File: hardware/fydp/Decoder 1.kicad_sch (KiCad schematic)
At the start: 26 parts, among them J21 Conn_01x04_Pin, J6 Conn_01x04_Pin, U4 74HC139N

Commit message: Did some work in class lol
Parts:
- removed J21, J6: Conn_01x04_Pin, Connector_PinHeader_2.54mm:PinHeader_1x04_P2.54mm_Vertical, symbol Connector:Conn_01x04_Pin
- added J8: Conn_01x08_Pin, Connector_PinHeader_2.54mm:PinHeader_1x08_P2.54mm_Vertical, symbol Connector:Conn_01x08_Pin
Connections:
- net +3.3V: now also J8.5 (Pin_5), J8.7 (Pin_7)
- net ADC_DECODER_A0: now also J8.2 (Pin_2)
- net ADC_DECODER_A1: now also J8.1 (Pin_1)
- net ADC_DECODER_EN_L: now also J8.6 (Pin_6)
- net DAC_IN_DECODER_A0: now also J8.4 (Pin_4)
- net DAC_IN_DECODER_A1: now also J8.3 (Pin_3)
- net DAC_IN_DECODER_EN_L: now also J8.8 (Pin_8)
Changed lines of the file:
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@@
 (kicad_sch (version 20230121) (generator eeschema)
   (paper "A4")
-  (junction (at 196.85 45.72) (diameter 0) (color 0 0 0 0)
-  )
   (junction (at 27.94 140.97) (diameter 0) (color 0 0 0 0)
   )
@@
   (junction (at 52.07 105.41) (diameter 0) (color 0 0 0 0)
   )
+  (junction (at 218.44 57.15) (diameter 0) (color 0 0 0 0)
+  )
   (junction (at 124.46 66.04) (diameter 0) (color 0 0 0 0)
   )
@@
     (stroke (width 0) (type default))
   )
-  (wire (pts (xy 196.85 50.8) (xy 198.12 50.8))
+  (wire (pts (xy 218.44 62.23) (xy 261.62 62.23))
     (stroke (width 0) (type default))
   )
@@
     (stroke (width 0) (type default))
   )
+  (wire (pts (xy 218.44 57.15) (xy 261.62 57.15))
+    (stroke (width 0) (type default))
+  )
   (wire (pts (xy 36.83 151.13) (xy 64.77 151.13))
     (stroke (width 0) (type default))
@@
     (stroke (width 0) (type default))
   )
-  (wire (pts (xy 175.26 48.26) (xy 198.12 48.26))
+  (wire (pts (xy 238.76 59.69) (xy 261.62 59.69))
     (stroke (width 0) (type default))
   )
@@
     (stroke (width 0) (type default))
   )
-  (wire (pts (xy 193.04 44.45) (xy 193.04 45.72))
+  (wire (pts (xy 218.44 44.45) (xy 218.44 57.15))
     (stroke (width 0) (type default))
   )
@@
     (stroke (width 0) (type default))
   )
-  (wire (pts (xy 196.85 45.72) (xy 196.85 50.8))
+  (wire (pts (xy 218.44 57.15) (xy 218.44 62.23))
     (stroke (width 0) (type default))
   )
@@
     (stroke (width 0) (type default))
   )
-  (wire (pts (xy 198.12 45.72) (xy 196.85 45.72))
-    (stroke (width 0) (type default))
-  )
   (wire (pts (xy 217.17 107.95) (xy 217.17 129.54))
     (stroke (width 0) (type default))
@@
     (stroke (width 0) (type default))
   )
-  (wire (pts (xy 196.85 45.72) (xy 193.04 45.72))
-    (stroke (width 0) (type default))
-  )
   (wire (pts (xy 74.93 130.81) (xy 72.39 130.81))
     (stroke (width 0) (type default))
@@
     (stroke (width 0) (type default))
   )
-  (wire (pts (xy 175.26 53.34) (xy 198.12 53.34))
+  (wire (pts (xy 238.76 64.77) (xy 261.62 64.77))
     (stroke (width 0) (type default))
   )
@@
     (stroke (width 0) (type default))
   )
-  (rectangle (start 213.36 31.75) (end 276.86 59.69)
+  (rectangle (start 213.36 31.75) (end 276.86 67.31)
     (stroke (width 0) (type default))
     (fill (type none))
@@
     (effects (font (size 1.27 1.27)) (justify left bottom))
   )
-  (label "ADC_DECODER_A0" (at 223.52 52.07 0) (fields_autoplaced)
-    (effects (font (size 1.27 1.27)) (justify left bottom))
-  )
   (label "ADC4_CS_L_R" (at 95.25 118.11 0) (fields_autoplaced)
     (effects (font (size 1.27 1.27)) (justify left bottom))
@@
     (effects (font (size 1.27 1.27)) (justify left bottom))
   )
-  (label "DAC_IN_DECODER_A0" (at 223.52 46.99 0) (fields_autoplaced)
-    (effects (font (size 1.27 1.27)) (justify left bottom))
-  )
   (label "ADC_DECODER_EN_L" (at 95.25 102.87 0) (fields_autoplaced)
     (effects (font (size 1.27 1.27)) (justify left bottom))
   )
+  (label "ADC_DECODER_A1" (at 223.52 46.99 0) (fields_autoplaced)
+    (effects (font (size 1.27 1.27)) (justify left bottom))
+  )
   (label "ADC2_CS_L_R" (at 95.25 113.03 0) (fields_autoplaced)
     (effects (font (size 1.27 1.27)) (justify left bottom))
@@
     (effects (font (size 1.27 1.27)) (justify left bottom))
   )
+  (label "DAC_IN_DECODER_A1" (at 223.52 52.07 0) (fields_autoplaced)
+    (effects (font (size 1.27 1.27)) (justify left bottom))
+  )
+  (label "ADC_DECODER_A0" (at 223.52 49.53 0) (fields_autoplaced)
+    (effects (font (size 1.27 1.27)) (justify left bottom))
+  )
   (label "DAC_IN3_CS_L_R" (at 184.15 110.49 0) (fields_autoplaced)
     (effects (font (size 1.27 1.27)) (justify left bottom))
@@
     (effects (font (size 1.27 1.27)) (justify left bottom))
   )
+  (label "DAC_IN_DECODER_A0" (at 223.52 54.61 0) (fields_autoplaced)
+    (effects (font (size 1.27 1.27)) (justify left bottom))
+  )
   (label "DAC_IN_DECODER_A1" (at 184.15 105.41 0) (fields_autoplaced)
     (effects (font (size 1.27 1.27)) (justify left bottom))
   )
-  (label "ADC_DECODER_EN_L" (at 175.26 48.26 0) (fields_autoplaced)
-    (effects (font (size 1.27 1.27)) (justify left bottom))
-  )
-  (label "ADC_DECODER_A1" (at 223.52 54.61 0) (fields_autoplaced)
+  (label "ADC_DECODER_EN_L" (at 238.76 59.69 0) (fields_autoplaced)
     (effects (font (size 1.27 1.27)) (justify left bottom))
   )
@@
     (effects (font (size 1.27 1.27)) (justify left bottom))
   )
-  (label "DAC_IN_DECODER_EN_L" (at 175.26 53.34 0) (fields_autoplaced)
-    (effects (font (size 1.27 1.27)) (justify left bottom))
-  )
-  (label "DAC_IN_DECODER_A1" (at 223.52 49.53 0) (fields_autoplaced)
+  (label "DAC_IN_DECODER_EN_L" (at 238.76 64.77 0) (fields_autoplaced)
     (effects (font (size 1.27 1.27)) (justify left bottom))
   )
@@
     )
   )
-  (symbol (lib_id "Connector:Conn_01x04_Pin") (at 266.7 49.53 0) (mirror y) (unit 1)
-    (in_bom yes) (on_board yes) (dnp no)
-    (property "Reference" "J6" (at 266.065 41.91 0)
-      (effects (font (size 1.27 1.27)))
-    )
-    (property "Value" "Conn_01x04_Pin" (at 266.065 44.45 0)
-      (effects (font (size 1.27 1.27)))
-    )
-    (property "Footprint" "Connector_PinHeader_2.54mm:PinHeader_1x04_P2.54mm_Vertical" (at 266.7 49.53 0)
-      (effects (font (size 1.27 1.27)) hide)
-    )
-    (property "Datasheet" "~" (at 266.7 49.53 0)
-      (effects (font (size 1.27 1.27)) hide)
-    )
-    (pin "1")
-    (pin "2")
-    (pin "3")
-    (pin "4")
-    (instances
-      (project "fydp"
-        (path "/2d5d1aad-2c7d-465e-90ef-822dec61a05e/81e437c6-75e9-4d17-8bc1-2d59c32a09ba"
-          (reference "J6") (unit 1)
-        )
-        (path "/2d5d1aad-2c7d-465e-90ef-822dec61a05e/3df3811f-49cf-4b83-bd7a-16254be775c2"
-          (reference "J8") (unit 1)
-        )
-      )
-    )
-  )
   (symbol (lib_id "Device:R") (at 68.58 161.29 270) (unit 1)
     (in_bom yes) (on_board yes) (dnp no)
@@
     )
   )
+  (symbol (lib_id "Connector:Conn_01x08_Pin") (at 266.7 54.61 0) (mirror y) (unit 1)
+    (in_bom yes) (on_board yes) (dnp no)
+    (property "Reference" "J8" (at 266.065 43.18 0)
+      (effects (font (size 1.27 1.27)))
+    )
+    (property "Value" "Conn_01x08_Pin" (at 266.065 45.72 0)
+      (effects (font (size 1.27 1.27)))
+    )
+    (property "Footprint" "Connector_PinHeader_2.54mm:PinHeader_1x08_P2.54mm_Vertical" (at 266.7 54.61 0)
+      (effects (font (size 1.27 1.27)) hide)
+    )
+    (property "Datasheet" "~" (at 266.7 54.61 0)
+      (effects (font (size 1.27 1.27)) hide)
+    )
+    (pin "1")
+    (pin "2")
+    (pin "3")
+    (pin "4")
+    (pin "5")
+    (pin "6")
+    (pin "7")
+    (pin "8")
+    (instances
+      (project "fydp"
+        (path "/2d5d1aad-2c7d-465e-90ef-822dec61a05e/3df3811f-49cf-4b83-bd7a-16254be775c2"
+          (reference "J8") (unit 1)
+        )
+      )
+    )
+  )
   (symbol (lib_id "power:GND") (at 45.72 180.34 0) (unit 1)
     (in_bom yes) (on_board yes) (dnp no) (fields_autoplaced)
@@
     )
   )
-  (symbol (lib_id "power:+3.3V") (at 193.04 44.45 0) (unit 1)
-    (in_bom yes) (on_board yes) (dnp no) (fields_autoplaced)
-    (property "Reference" "#PWR013" (at 193.04 48.26 0)
-      (effects (font (size 1.27 1.27)) hide)
-    )
-    (property "Value" "+3.3V" (at 193.04 39.37 0)
-      (effects (font (size 1.27 1.27)))
-    )
-    (property "Footprint" "" (at 193.04 44.45 0)
-      (effects (font (size 1.27 1.27)) hide)
-    )
-    (property "Datasheet" "" (at 193.04 44.45 0)
+  (symbol (lib_id "power:+3.3V") (at 218.44 44.45 0) (unit 1)
+    (in_bom yes) (on_board yes) (dnp no) (fields_autoplaced)
+    (property "Reference" "#PWR013" (at 218.44 48.26 0)
+      (effects (font (size 1.27 1.27)) hide)
+    )
+    (property "Value" "+3.3V" (at 218.44 39.37 0)
+      (effects (font (size 1.27 1.27)))
+    )
+    (property "Footprint" "" (at 218.44 44.45 0)
+      (effects (font (size 1.27 1.27)) hide)
+    )
+    (property "Datasheet" "" (at 218.44 44.45 0)
       (effects (font (size 1.27 1.27)) hide)
     )
@@
         )
       )
-    )
-  )
-  (symbol (lib_id "Connector:Conn_01x04_Pin") (at 203.2 48.26 0) (mirror y) (unit 1)
-    (in_bom yes) (on_board yes) (dnp no)
-    (property "Reference" "J21" (at 202.565 40.64 0)
-      (effects (font (size 1.27 1.27)))
-    )
-    (property "Value" "Conn_01x04_Pin" (at 202.565 43.18 0)
-      (effects (font (size 1.27 1.27)))
-    )
-    (property "Footprint" "Connector_PinHeader_2.54mm:PinHeader_1x04_P2.54mm_Vertical" (at 203.2 48.26 0)
-      (effects (font (size 1.27 1.27)) hide)
-    )
-    (property "Datasheet" "~" (at 203.2 48.26 0)
-      (effects (font (size 1.27 1.27)) hide)
-    )
-    (pin "1")
-    (pin "2")
-    (pin "3")
-    (pin "4")
-    (instances
-      (project "fydp"
-        (path "/2d5d1aad-2c7d-465e-90ef-822dec61a05e/81e437c6-75e9-4d17-8bc1-2d59c32a09ba"
-          (reference "J21") (unit 1)
-        )
-        (path "/2d5d1aad-2c7d-465e-90ef-822dec61a05e/3df3811f-49cf-4b83-bd7a-16254be775c2"
-          (reference "J13") (unit 1)
-        )
-      )

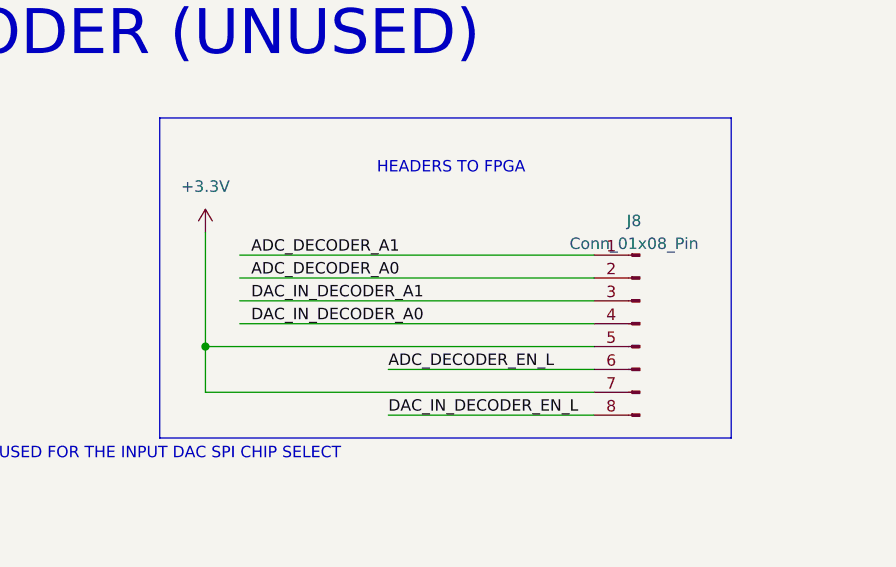
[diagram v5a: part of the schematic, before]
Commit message: Initial layout is pretty much complete, need to add power planes
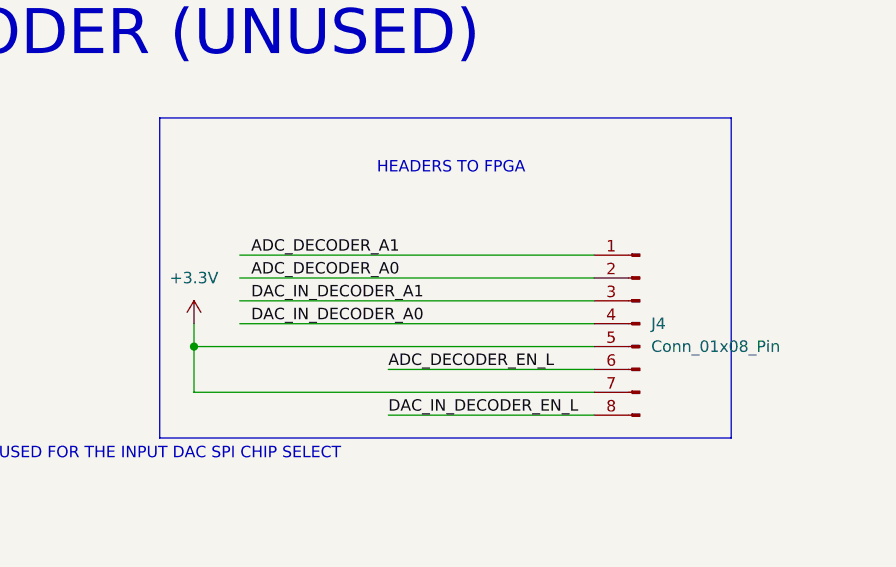
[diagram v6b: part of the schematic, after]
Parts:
- removed J8: Conn_01x08_Pin, Connector_PinHeader_2.54mm:PinHeader_1x08_P2.54mm_Vertical, symbol Connector:Conn_01x08_Pin
- added J4: Conn_01x08_Pin, Connector_PinHeader_2.54mm:PinHeader_1x08_P2.54mm_Vertical, symbol Connector:Conn_01x08_Pin
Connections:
- net +3.3V: now also J4.5 (Pin_5), J4.7 (Pin_7)
- net ADC_DECODER_A0: now also J4.2 (Pin_2)
- net ADC_DECODER_A1: now also J4.1 (Pin_1)
- net ADC_DECODER_EN_L: now also J4.6 (Pin_6)
- net DAC_IN_DECODER_A0: now also J4.4 (Pin_4)
- net DAC_IN_DECODER_A1: now also J4.3 (Pin_3)
- net DAC_IN_DECODER_EN_L: now also J4.8 (Pin_8)

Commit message: Adding JLCPCB BOM notes
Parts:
- C2: Comment (none) -> 0.1 µF ±10% 50V Ceramic Capacitor X7R 0805 (2012 Metric); LCSC (none) -> C49678; MPN (none) -> CC0805KRX7R9BB104
- R1: Comment (none) -> 4.7 kOhms ±1% 0.125W, 1/8W Chip Resistor 0805 (2012 Metric)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; LCSC (none) -> C60816; MPN (none) -> RC0805FR-074K7L
- R49, R62: Comment (none) -> 100 Ohms ±1% 0.125W, 1/8W Chip Resistor 0805 (2012 Metric) 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; LCSC (none) -> C105577; MPN (none) -> RC0805FR-07100RL

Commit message: Updating BOM some more
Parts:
- J4: Comment (none) -> Connector Header Through Hole 8 position 0.100" (2.54mm); MPN (none) -> TSW-108-07-G-S
- U4: MPN (none) -> 74HC139N
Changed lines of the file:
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@@
       (effects (font (size 1.27 1.27)) hide)
     )
-    (property "Datasheet" "~" (at 266.7 54.61 0)
+    (property "Datasheet" "https://suddendocs.samtec.com/catalog_english/tsw_th.pdf" (at 266.7 54.61 0)
+      (effects (font (size 1.27 1.27)) hide)
+    )
+    (property "Comment" "Connector Header Through Hole 8 position 0.100\" (2.54mm)" (at 266.7 54.61 0)
+      (effects (font (size 1.27 1.27)) hide)
+    )
+    (property "MPN" "TSW-108-07-G-S" (at 266.7 54.61 0)
       (effects (font (size 1.27 1.27)) hide)
     )
@@
       (effects (font (size 1.27 1.27) italic) hide)
     )
-    (pin "1")
+    (property "MPN" "74HC139N" (at 181.61 100.33 0)
+      (effects (font (size 1.27 1.27)) hide)
+    )
+    (pin "1")
